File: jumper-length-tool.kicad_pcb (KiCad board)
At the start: 2 copper layers, 43.9 x 112.9 mm, 3 parts

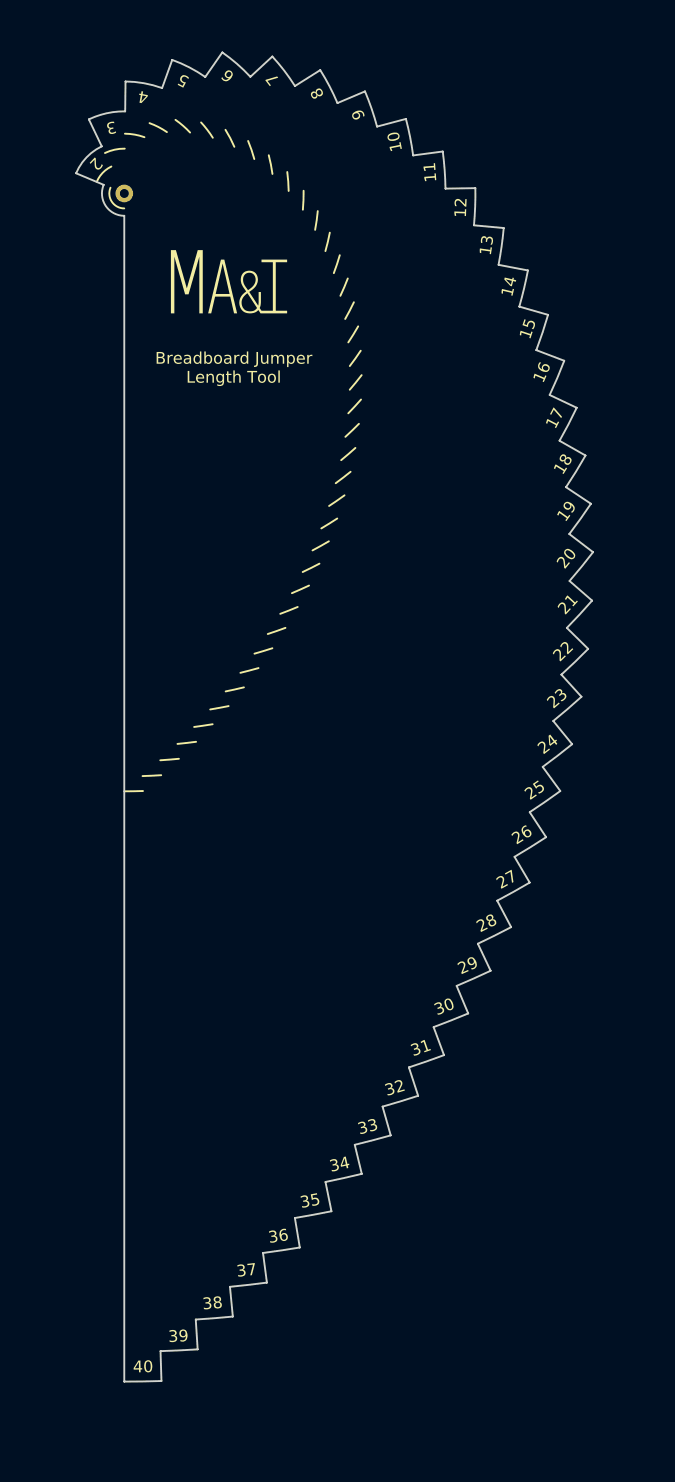
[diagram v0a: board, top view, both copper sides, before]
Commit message: Add copper fill
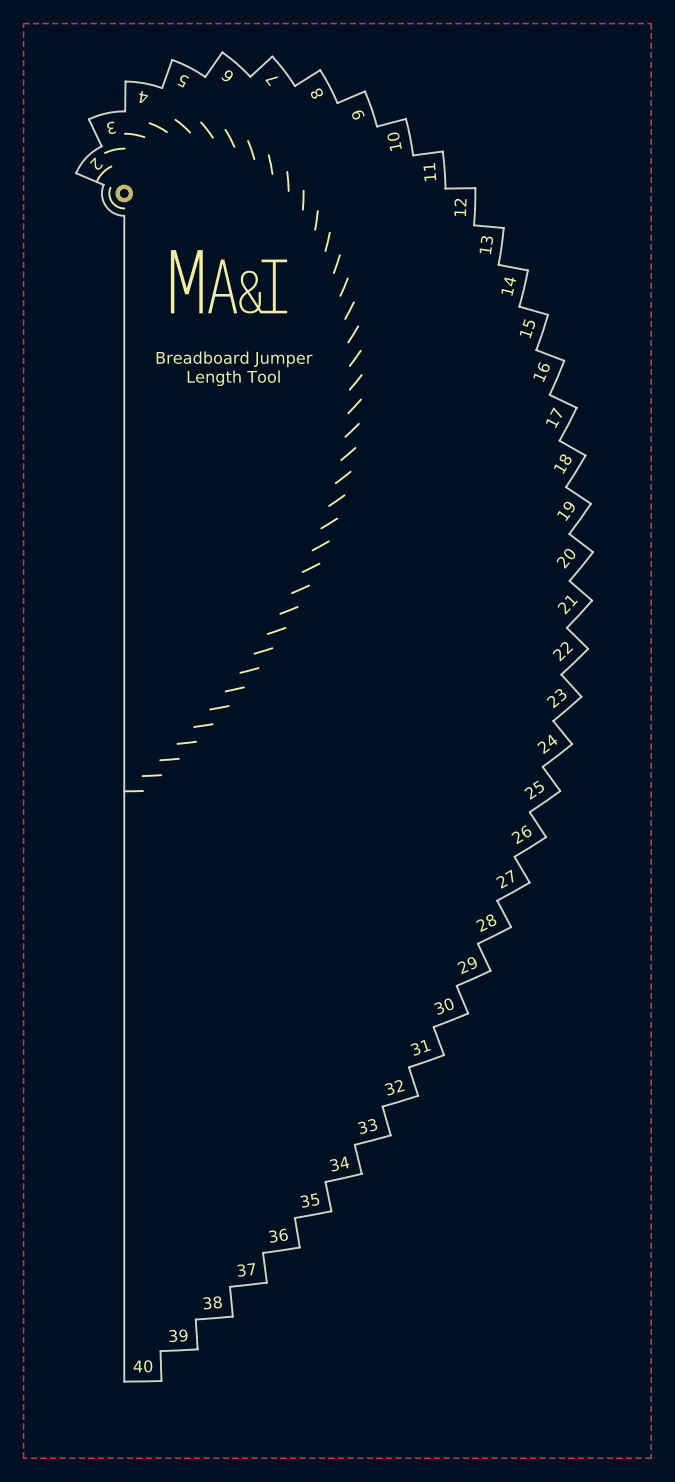
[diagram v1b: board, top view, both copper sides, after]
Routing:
- added copper zone on B.Cu, net (none)
- added copper zone on F.Cu, net (none)
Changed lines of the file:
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@@
 			(plot_on_all_layers_selection 0x00000000_00000000_00000000_00000000)
 			(disableapertmacros no)
-			(usegerberextensions no)
+			(usegerberextensions yes)
 			(usegerberattributes yes)
 			(usegerberadvancedattributes yes)
@@
 			(outputformat 1)
 			(mirror no)
-			(drillshape 1)
+			(drillshape 0)
 			(scaleselection 1)
-			(outputdirectory "")
+			(outputdirectory "gerbers")
 		)
 	)
@@
 		)
 	)
+	(zone
+		(net 0)
+		(net_name "")
+		(layers "F.Cu" "B.Cu")
+		(hatch edge 0.5)
+		(connect_pads
+			(clearance 0.5)
+		)
+		(min_thickness 0.25)
+		(filled_areas_thickness no)
+		(fill yes
+			(thermal_gap 0.5)
+			(thermal_bridge_width 0.5)
+			(island_removal_mode 1)
+			(island_area_min 10)
+		)
+		(polygon
+			(pts
+				(xy 91.44 35.56) (xy 144.78 35.56) (xy 144.78 157.48) (xy 91.44 157.48)
+			)
+		)
+	)

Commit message: Fix dimensions and add guide lines
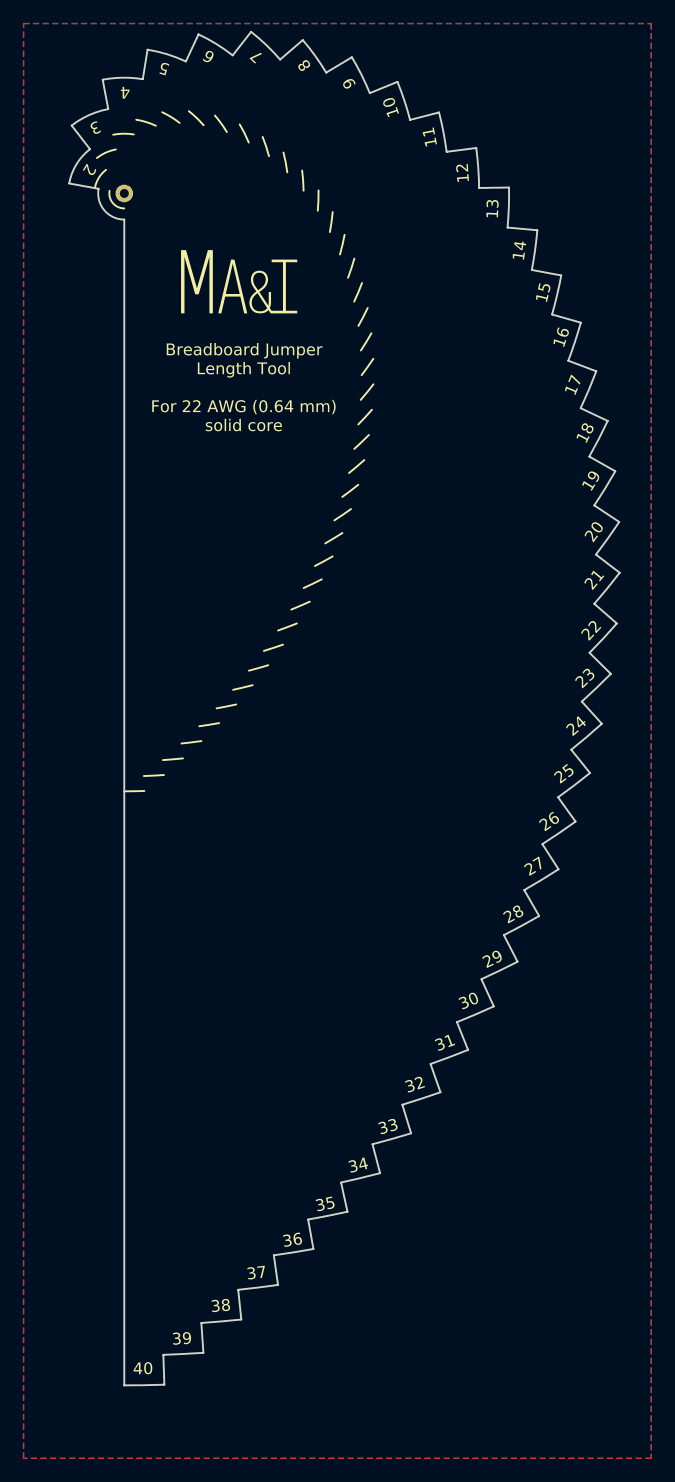
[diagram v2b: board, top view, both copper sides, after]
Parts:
- moved REF** 0.86 mm to (109.8, 57.5) (x2)
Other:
- board size 43.9 x 112.9 mm -> 46.8 x 115 mm
- board text added: "Breadboard Jumper Length Tool For 22 AWG (0.64 mm) solid core"
- board text removed: "Breadboard Jumper Length Tool"
